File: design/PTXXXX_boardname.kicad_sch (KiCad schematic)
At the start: 11 parts

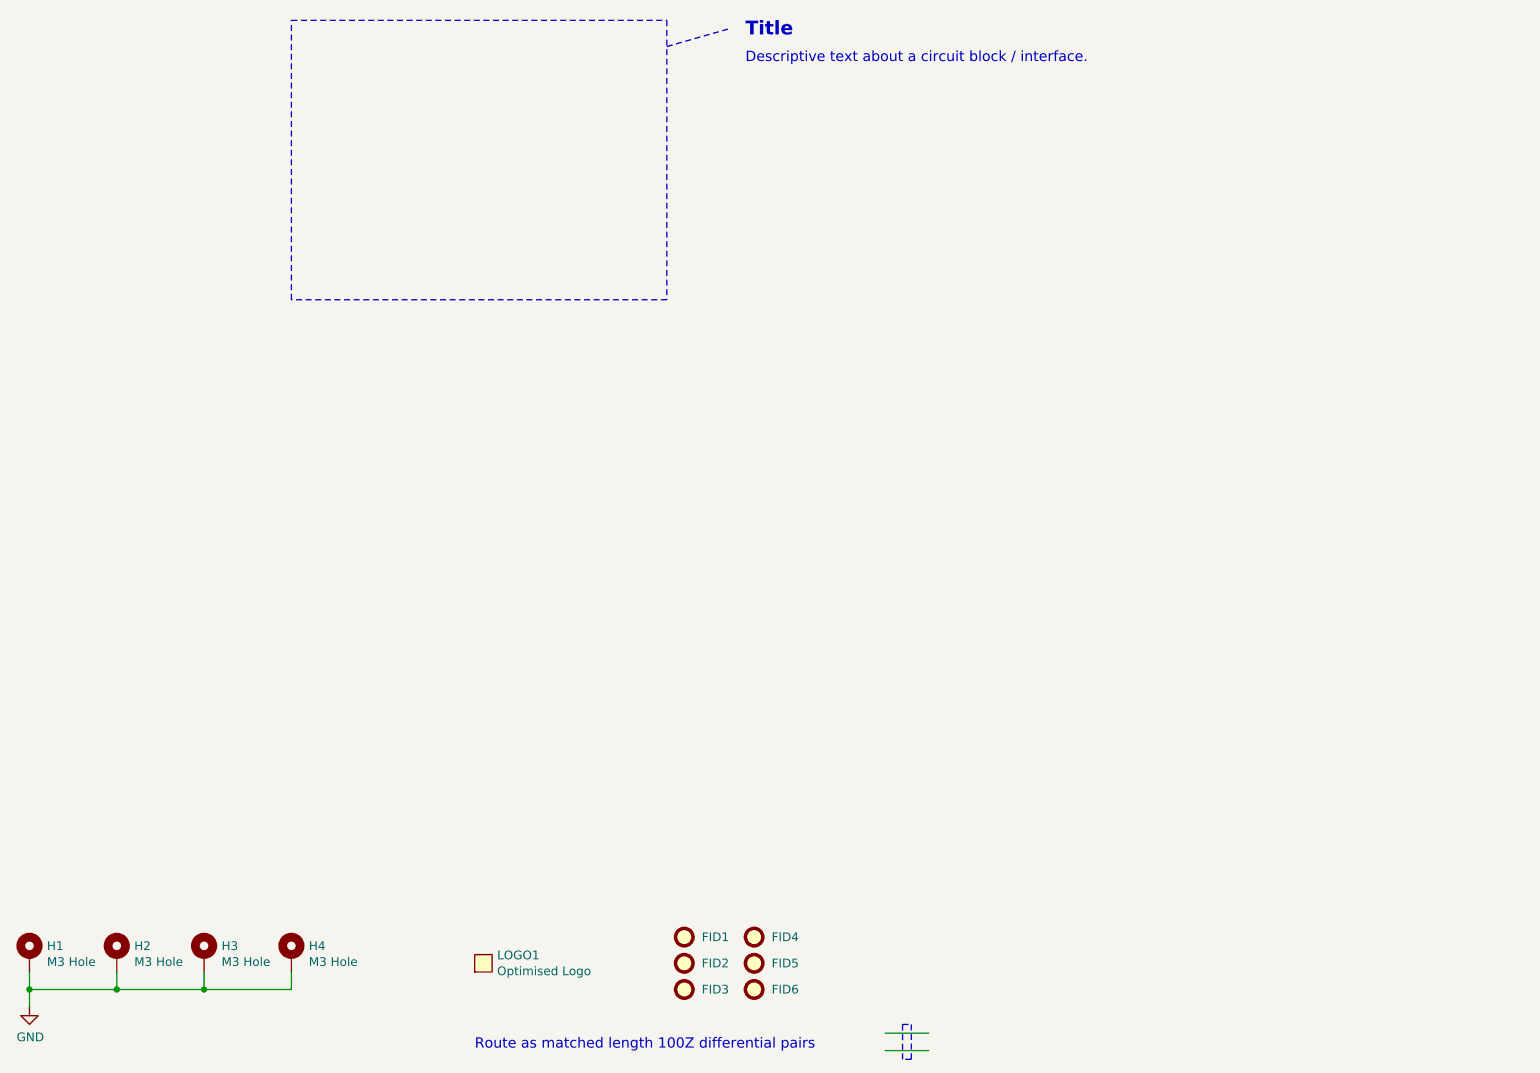
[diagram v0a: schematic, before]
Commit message: QoL Quality of Life changes: added extra readme titleblock space added customer logo part arrange BOM order in schematic symbol fields table added GND test point styles (hole and pad) reduced soldermask expansion from 0.065mm to 0.05mm changed copper-to-hole from 0.5mm to 0.35mm removed 0.5/0.9mm via size adjusted teardrop rules to better sizes update library reference
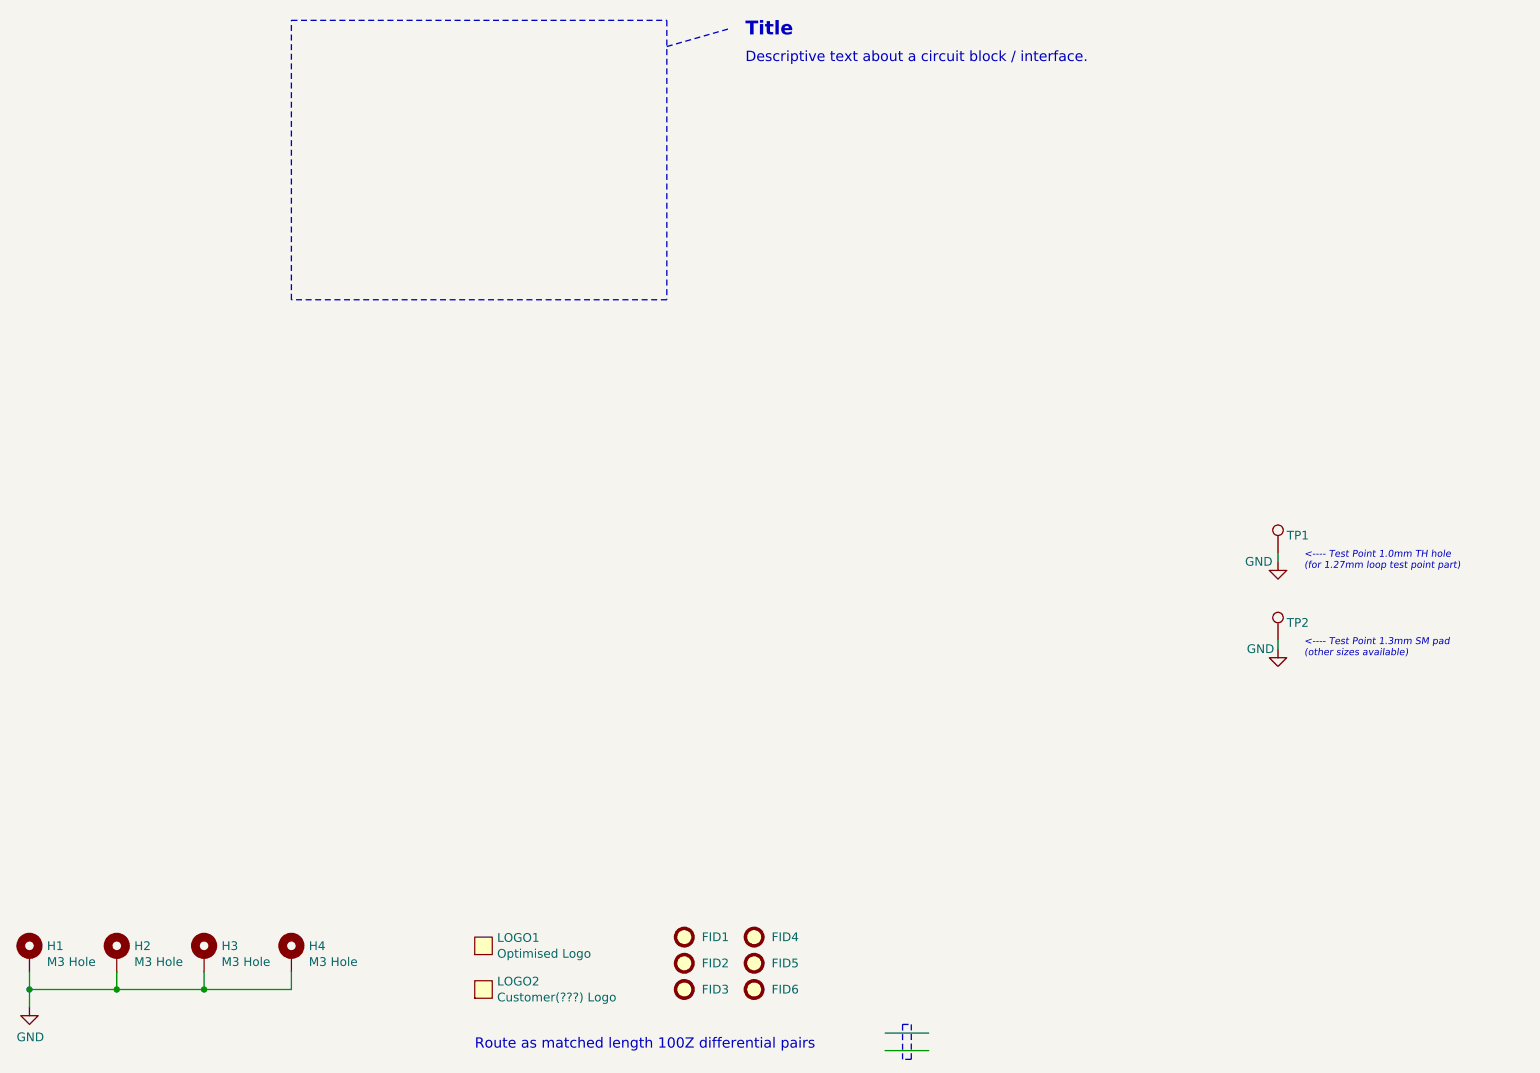
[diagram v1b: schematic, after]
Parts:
- added LOGO2: Customer(???) Logo, ???, symbol _kb_miscellaneous:Logo
- added TP1: TestPoint_TH_Loop_1.27mm_Keystone_5001, _kb_miscellaneous:TestPoint_TH_Loop_1.27mm_Keystone_5001, symbol _kb_miscellaneous:TestPoint_TH_Loop_1.27mm_Keystone_5001
- added TP2: TestPoint_Pad_1.3mm, _kb_miscellaneous:TestPoint_Pad_1.3mm, symbol _kb_miscellaneous:TestPoint_Pad_1.3mm
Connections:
- net GND: now also TP1.1, TP2.1
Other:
- note added: "<---- Test Point 1.0mm TH hole (for 1.27mm loop test point part)"
- note added: "<---- Test Point 1.3mm SM pad (other sizes available)"
- moved on the sheet: LOGO1
